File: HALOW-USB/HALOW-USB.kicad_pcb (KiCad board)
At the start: 2 copper layers, 15 x 32 mm, 12 parts, among them U1 TLV75533PDBVR, U2 GT-USB-7010ASV

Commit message: trace work
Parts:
- added R2: 5k1, Resistor_SMD:R_0603_1608Metric_Pad0.98x0.95mm_HandSolder, F.Cu at (118.5, 103.5)
- added R3: 5k1, Resistor_SMD:R_0603_1608Metric_Pad0.98x0.95mm_HandSolder, F.Cu at (128.5, 103.5)
- added U3: USBLC6-2SC6, Package_TO_SOT_SMD:SOT-23-6, F.Cu at (123.5, 101.3)
- moved U2 9.39 mm to (123.5, 108.4)
- moved C5 6.76 mm to (118.5, 101.5), turned to 0 degrees
- moved U1 6.12 mm to (118.5, 98.5), turned to -90 degrees
- moved C6 4.91 mm to (118.5, 95.5), turned to 0 degrees
- moved R1 3.00 mm to (124.8, 78.5)
- moved C7 1.70 mm to (124.8, 76.5)
- moved MM8108-MF1 1.14 mm to (118.5, 80.5)
- moved C1 1.12 mm to (127.5, 77.5)
- moved JP1 1.00 mm to (119.5, 77.5)
- moved C3 0.50 mm to (128.5, 92.8)
- moved C4 0.10 mm to (124.5, 92.8)
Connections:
- net /5v_in renamed +5V
- MM8108-MF1 pad 27: USB_D- -> /USB/USB D-
- MM8108-MF1 pad 28: USB_D+ -> /USB/USB_D+
- U2 pad A5: unconnected-(U2-CC1-PadA5) -> Net-(U2-CC1)
- U2 pad A6: USB_D+ -> /USB/PRE D+
- U2 pad A7: USB_D- -> /USB/PRE D-
- U2 pad B5: unconnected-(U2-CC2-PadB5) -> Net-(U2-CC2)
- U2 pad B6: USB_D+ -> /USB/PRE D+
- U2 pad B7: USB_D- -> /USB/PRE D-
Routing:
- net +3.3V: track 34.2 -> 0.00 mm
- net +5V: track 3.43 -> 20.5 mm, vias 0 -> 2
- net USB_D-: track 11.3 -> 0.00 mm, vias 2 -> 0
- net USB_D+: track 10.9 -> 0.00 mm, vias 2 -> 0
- net /USB/PRE D+: track 0.00 -> 8.26 mm, vias 0 -> 2
- net /USB/PRE D-: track 0.00 -> 7.15 mm, vias 0 -> 2
- net /reset: track 5.76 -> 0.00 mm
- net Net-(U2-CC1): track 0.00 -> 4.40 mm
- net Net-(U2-CC2): track 0.00 -> 3.84 mm
- net GND: track 3.75 -> 0.00 mm
- net /RF_OUT: track 2.69 -> 0.00 mm
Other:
- board size 15 x 32 mm -> 25 x 45 mm

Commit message: mfg files added
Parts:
- added G***: LOGO, LOGO, B.Cu at (123.2, 95.0)
- moved C1 3.73 mm to (127.0, 81.2)
- moved C7 3.73 mm to (124.3, 80.2)
- moved MM8108-MF1 3.73 mm to (118.0, 84.2)
- moved R1 3.73 mm to (124.3, 82.2)
- moved C2 3.26 mm to (126.7, 96.1)
- moved C3 3.26 mm to (128.6, 96.1)
- moved C4 3.26 mm to (124.6, 96.1)
- moved JP1 2.55 mm to (119.0, 80.0)
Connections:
- net /USB/USB D- renamed /D -
- net /USB/USB_D+ renamed /D +
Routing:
- net +3.3V: track 0.00 -> 43.0 mm, vias 0 -> 2
- net /D +: track 0.00 -> 8.91 mm, vias 0 -> 2
- net /D -: track 0.00 -> 8.91 mm, vias 0 -> 2
- net /reset: track 0.00 -> 5.59 mm
- net /RF_OUT: track 0.00 -> 5.26 mm
- net +5V: track 20.5 -> 24.0 mm, vias 2 -> 3
- net GND: vias 0 -> 120
- added copper zone on B.Cu, net GND
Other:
- board size 25 x 45 mm -> 16 x 37.5 mm
- board text added: "MAX WAS hErE"
- board text added: "R01. HOTPINK"

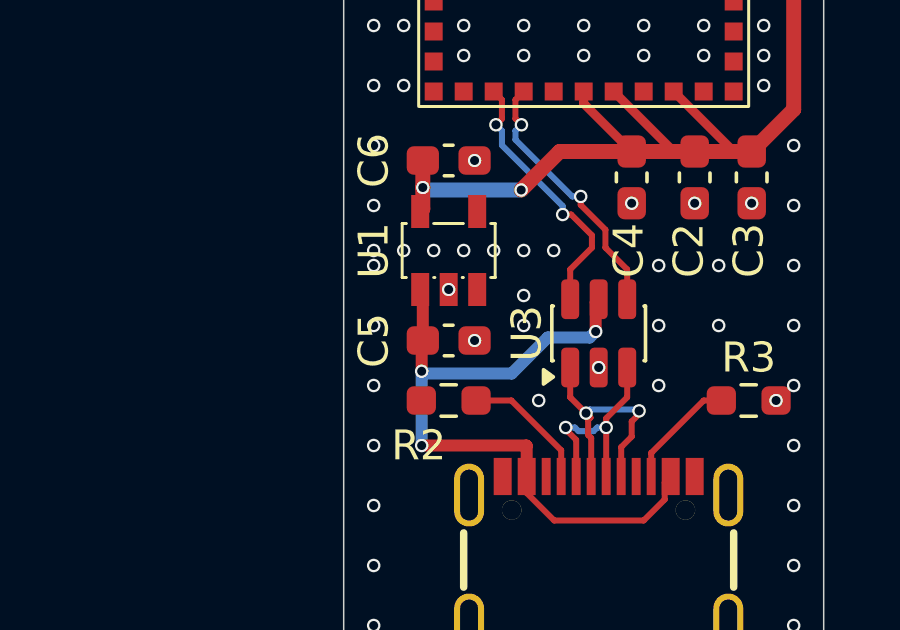
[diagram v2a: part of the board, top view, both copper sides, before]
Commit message: added 5v enable and stp export
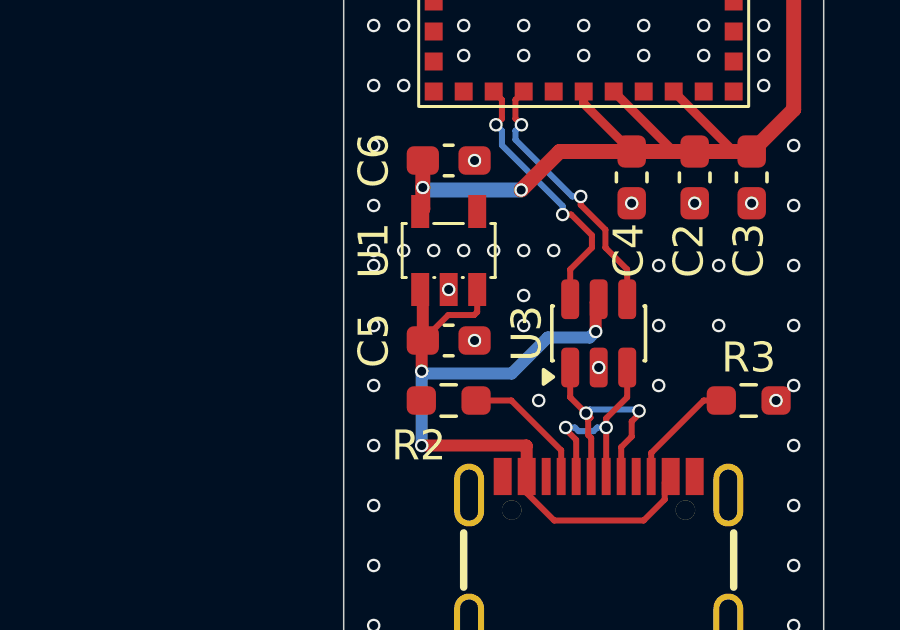
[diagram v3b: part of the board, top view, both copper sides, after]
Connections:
- U1 pad 3: unconnected-(U1-EN-Pad3) -> +5V
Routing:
- net +5V: track 24.0 -> 26.9 mm
